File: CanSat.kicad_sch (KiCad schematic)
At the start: 46 parts, among them IC1 W25Q128JVPIQ, J1 USB_C_Receptacle, J10 Conn_01x04_Pin, J2 Conn_Coaxial, J3 Conn_01x06_Socket, J4 Conn_01x02_Pin, J5 Screw_Terminal_01x02, J6 Conn_01x06_Pin, J7 Conn_01x03_Pin, J8 Conn_01x02_Pin, J9 Conn_01x02_Pin, SW1 SW_Push, SW2 SW_Push, SW3 SW_Push, U1 MPU-6050, U3 Waveshare23721, U4 RFM98W-433S2, U8 BMP280, U9 APS6404L-3SQR-ZR

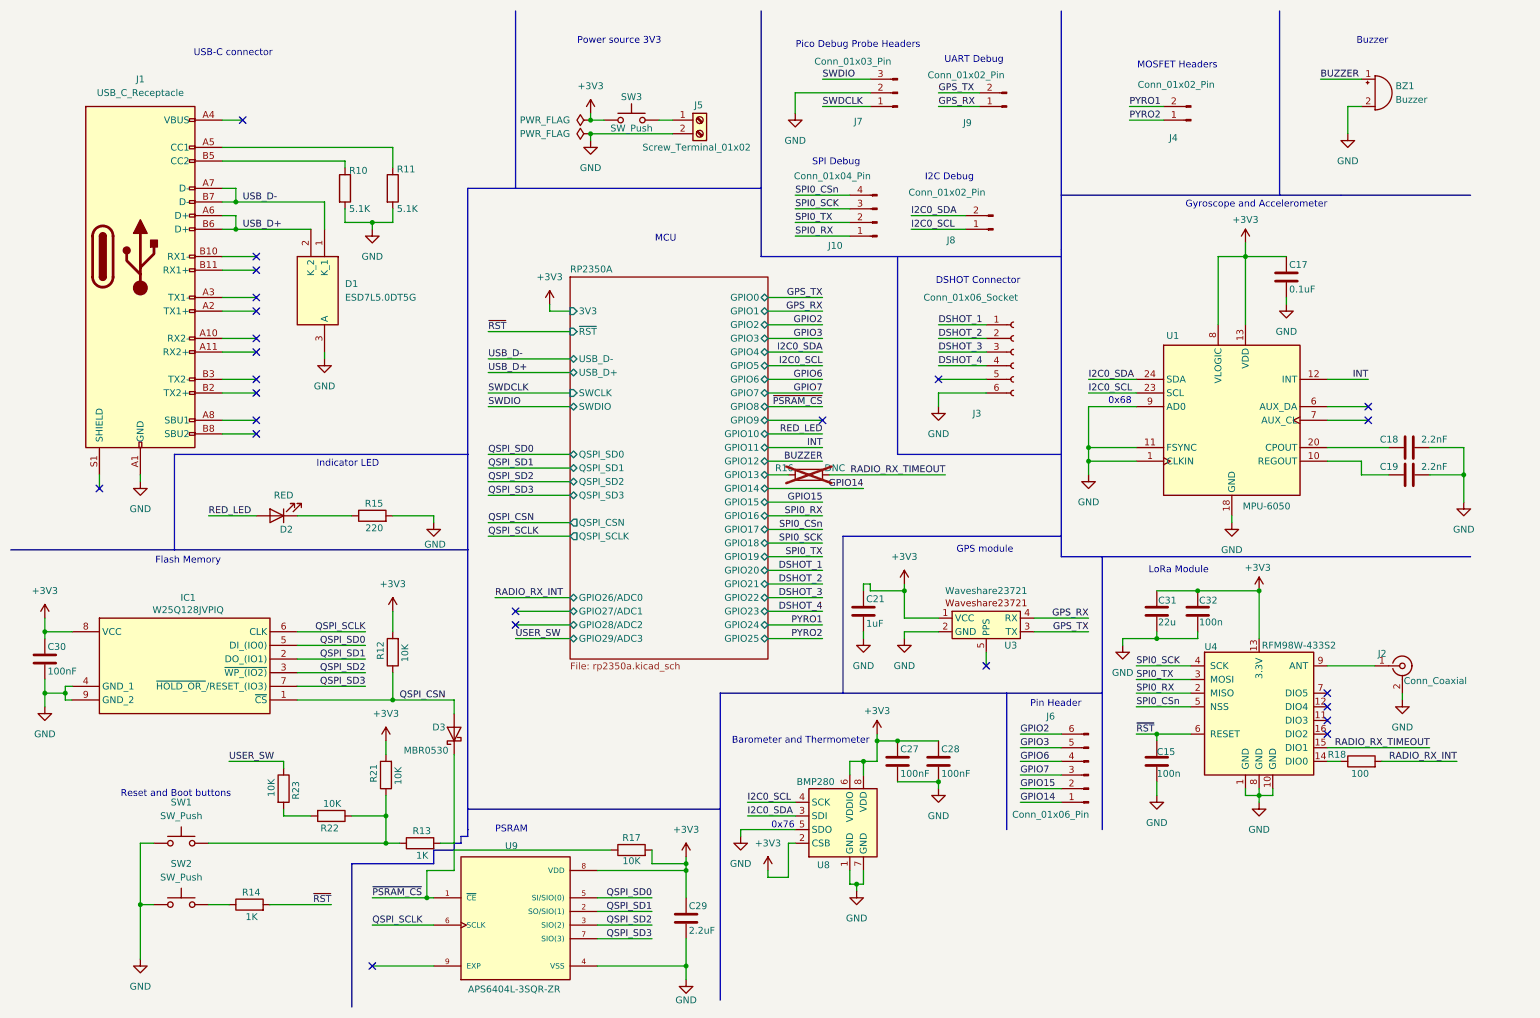
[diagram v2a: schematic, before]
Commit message: Changed connectors
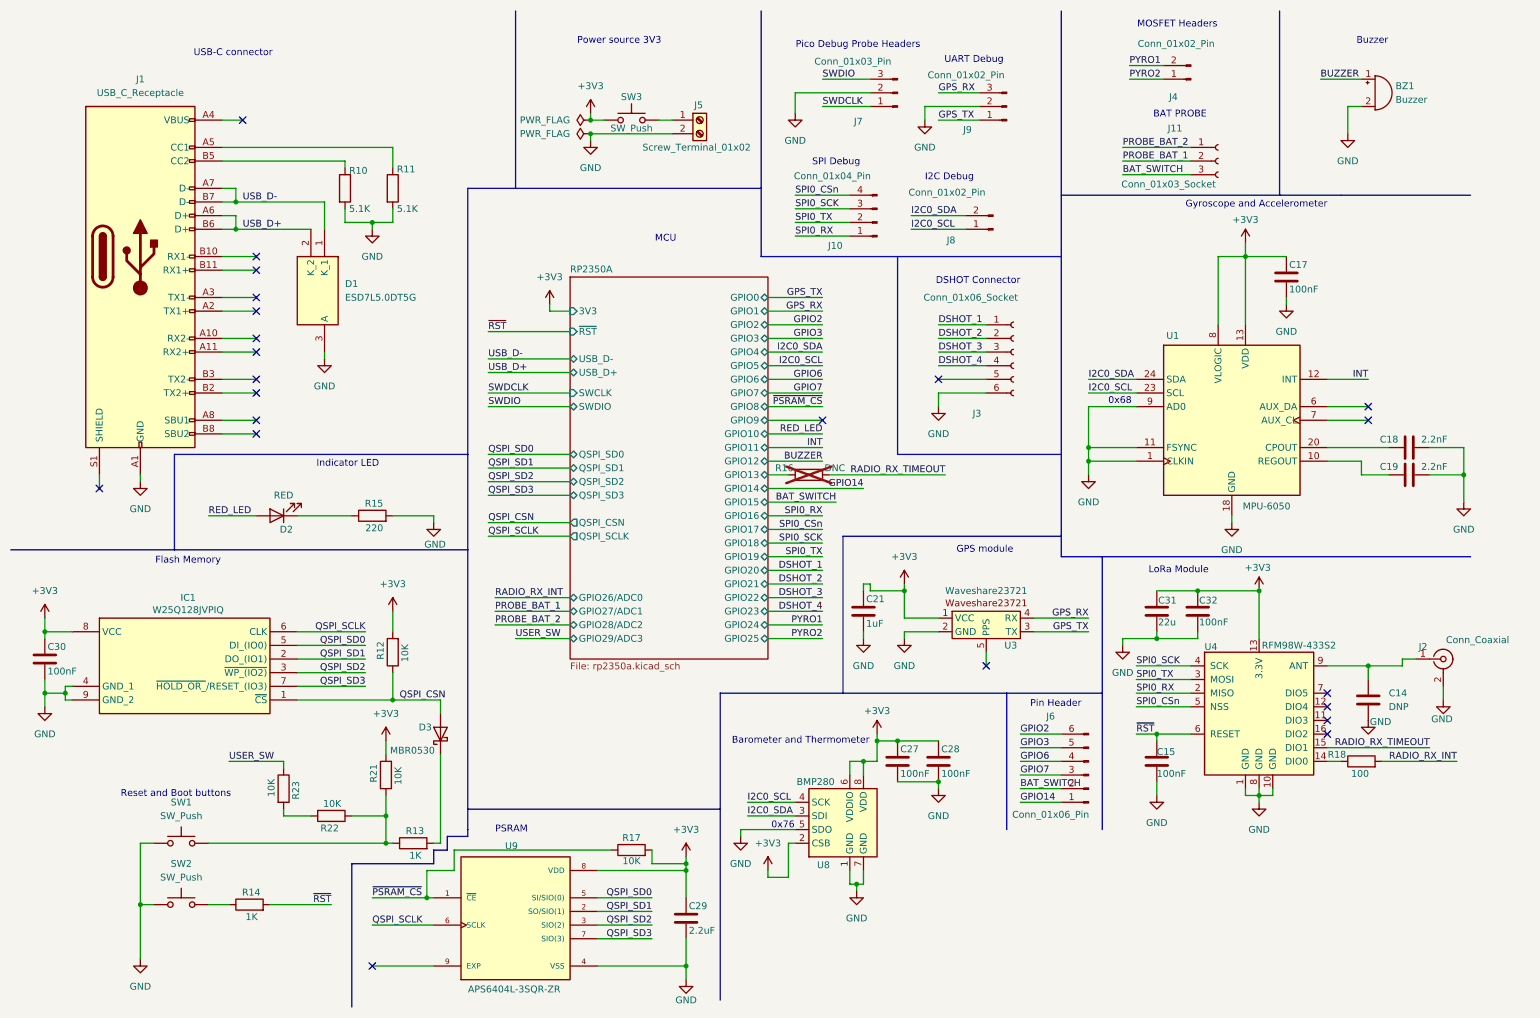
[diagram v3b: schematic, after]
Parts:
- added C14: DNP, Capacitor_SMD:C_0805_2012Metric, symbol Device:C
- added J11: Conn_01x03_Socket, Connector_JST:JST_PH_B3B-PH-K_1x03_P2.00mm_Vertical, symbol Connector:Conn_01x03_Socket
- C15, C32: value 100n -> 100nF
- C17: value 0.1uF -> 100nF
- J10: footprint Connector_PinHeader_1.00mm:PinHeader_1x04_P1.00mm_Vertical -> Connector_PinHeader_2.00mm:PinHeader_1x04_P2.00mm_Vertical
- J4: footprint Connector_PinHeader_1.00mm:PinHeader_1x02_P1.00mm_Vertical -> Connector_JST:JST_PH_B2B-PH-K_1x02_P2.00mm_Vertical
- J5: footprint TerminalBlock:TerminalBlock_bornier-2_P5.08mm -> Connector_JST:JST_PH_B2B-PH-K_1x02_P2.00mm_Vertical
- J7: footprint Connector_PinHeader_1.00mm:PinHeader_1x03_P1.00mm_Vertical -> Connector_JST:JST_SH_BM03B-SRSS-TB_1x03-1MP_P1.00mm_Vertical
- J8: footprint Connector_PinHeader_1.00mm:PinHeader_1x02_P1.00mm_Vertical -> Connector_PinHeader_2.00mm:PinHeader_1x02_P2.00mm_Vertical
- J9: footprint Connector_PinHeader_1.00mm:PinHeader_1x02_P1.00mm_Vertical -> Connector_JST:JST_SH_BM03B-SRSS-TB_1x03-1MP_P1.00mm_Vertical; symbol Connector:Conn_01x02_Pin -> Connector:Conn_01x03_Pin
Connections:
- net GND: now also J9.2 (Pin_2), C14.1
- net GPS_RX: now also J9.3 (Pin_3); no longer J9.1 (Pin_1)
- net GPS_TX: now also J9.1 (Pin_1); no longer J9.2 (Pin_2)
- net at J2.1 (In), U4.9 (ANT): now also C14.2
- net GPIO15 renamed BAT_SWITCH
- net BAT_SWITCH: now also J11.3 (Pin_3)
- new net PROBE_BAT_1: J11.2 (Pin_2)
- new net PROBE_BAT_2: J11.1 (Pin_1)
- no-connect marks 24 -> 22
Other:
- note added: "BAT PROBE"
- moved on the sheet: D3, J2, J4, R13

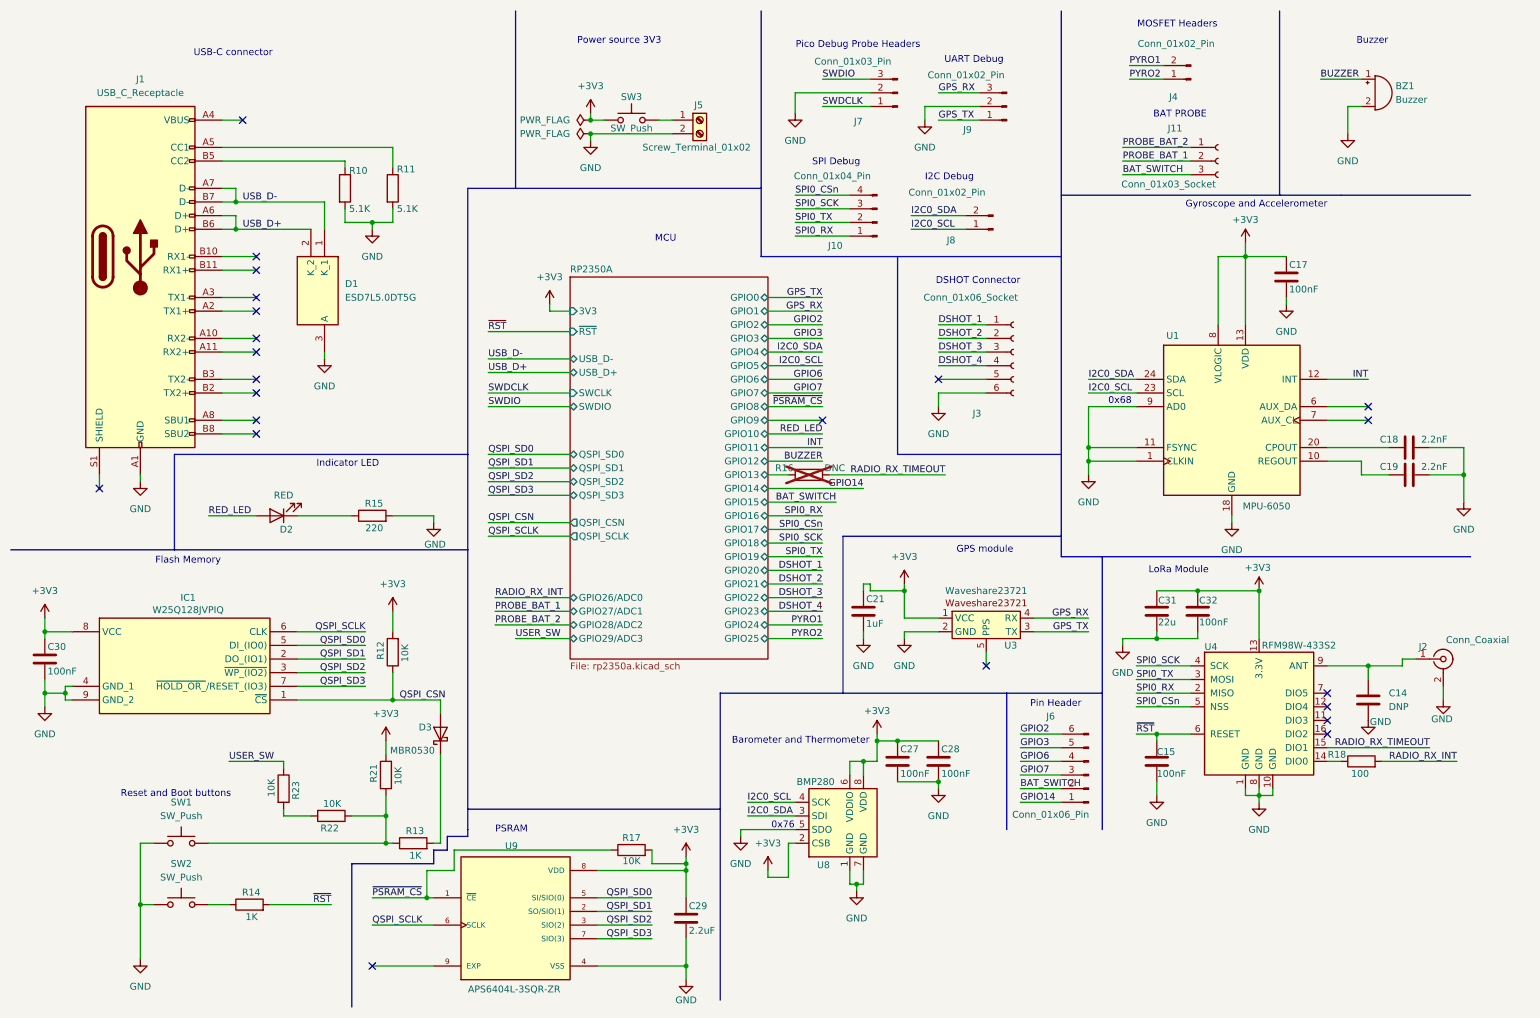
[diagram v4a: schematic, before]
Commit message: changed buzzer circuit and capacitor footprints
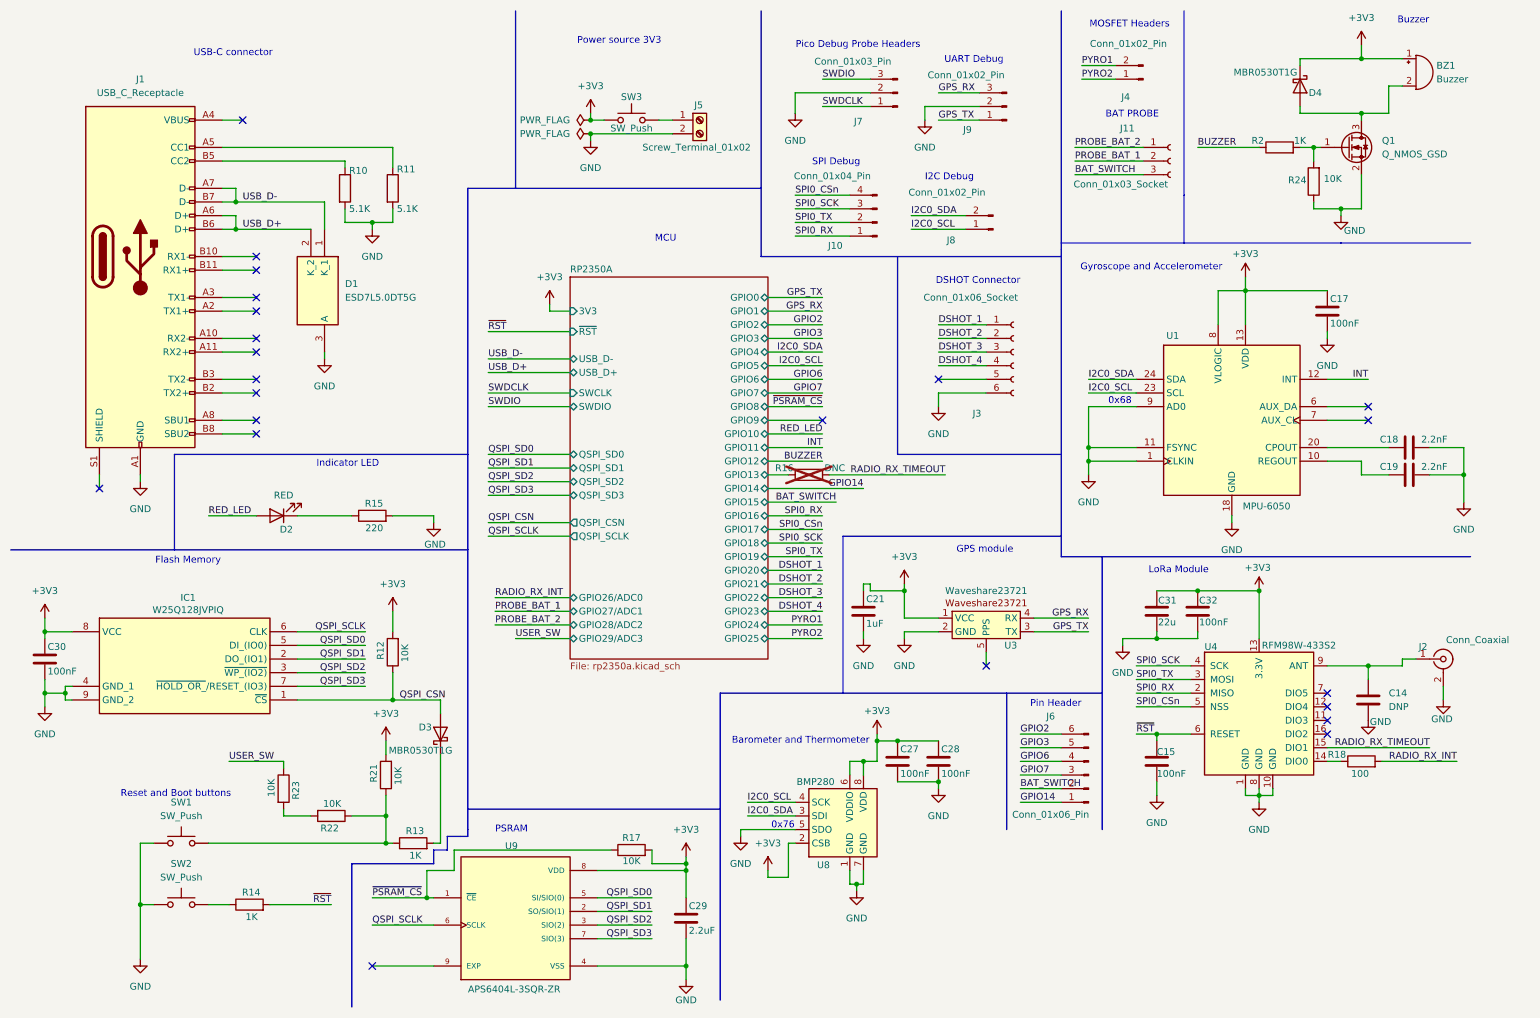
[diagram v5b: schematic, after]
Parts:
- added D4: MBR0530T1G, Diode_SMD:D_SOD-123, symbol Diode:MBR0530
- added Q1: Q_NMOS_GSD, Package_TO_SOT_SMD:SOT-23, symbol Transistor_FET:Q_NMOS_GSD
- added R2: 1K, Resistor_SMD:R_0805_2012Metric, symbol Device:R
- added R24: 10K, Resistor_SMD:R_0805_2012Metric, symbol Device:R
- C15, C17, C18, C19, C21, C27, C28, C29, C30, C31, C32: footprint Capacitor_Tantalum_SMD:CP_EIA-2012-15_AVX-P -> Capacitor_SMD:C_0805_2012Metric
- D3: value MBR0530 -> MBR0530T1G
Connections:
- net +3V3: now also BZ1.1 (+), D4.1 (K)
- net BUZZER: now also R2.1; no longer BZ1.1 (+)
- net GND: now also Q1.2 (S), R24.1; no longer BZ1.2 (-)
- new net: BZ1.2 (-), D4.2 (A), Q1.3 (D)
- new net: Q1.1 (G), R2.2, R24.2
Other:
- moved on the sheet: BZ1, C17, J11, J4

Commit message: added Q1 part number
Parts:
- Q1: value Q_NMOS_GSD -> BSS138
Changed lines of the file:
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@@
 			)
 		)
-		(property "Value" "Q_NMOS_GSD"
+		(property "Value" "BSS138"
 			(at 267.97 39.3699 0)
 			(effects

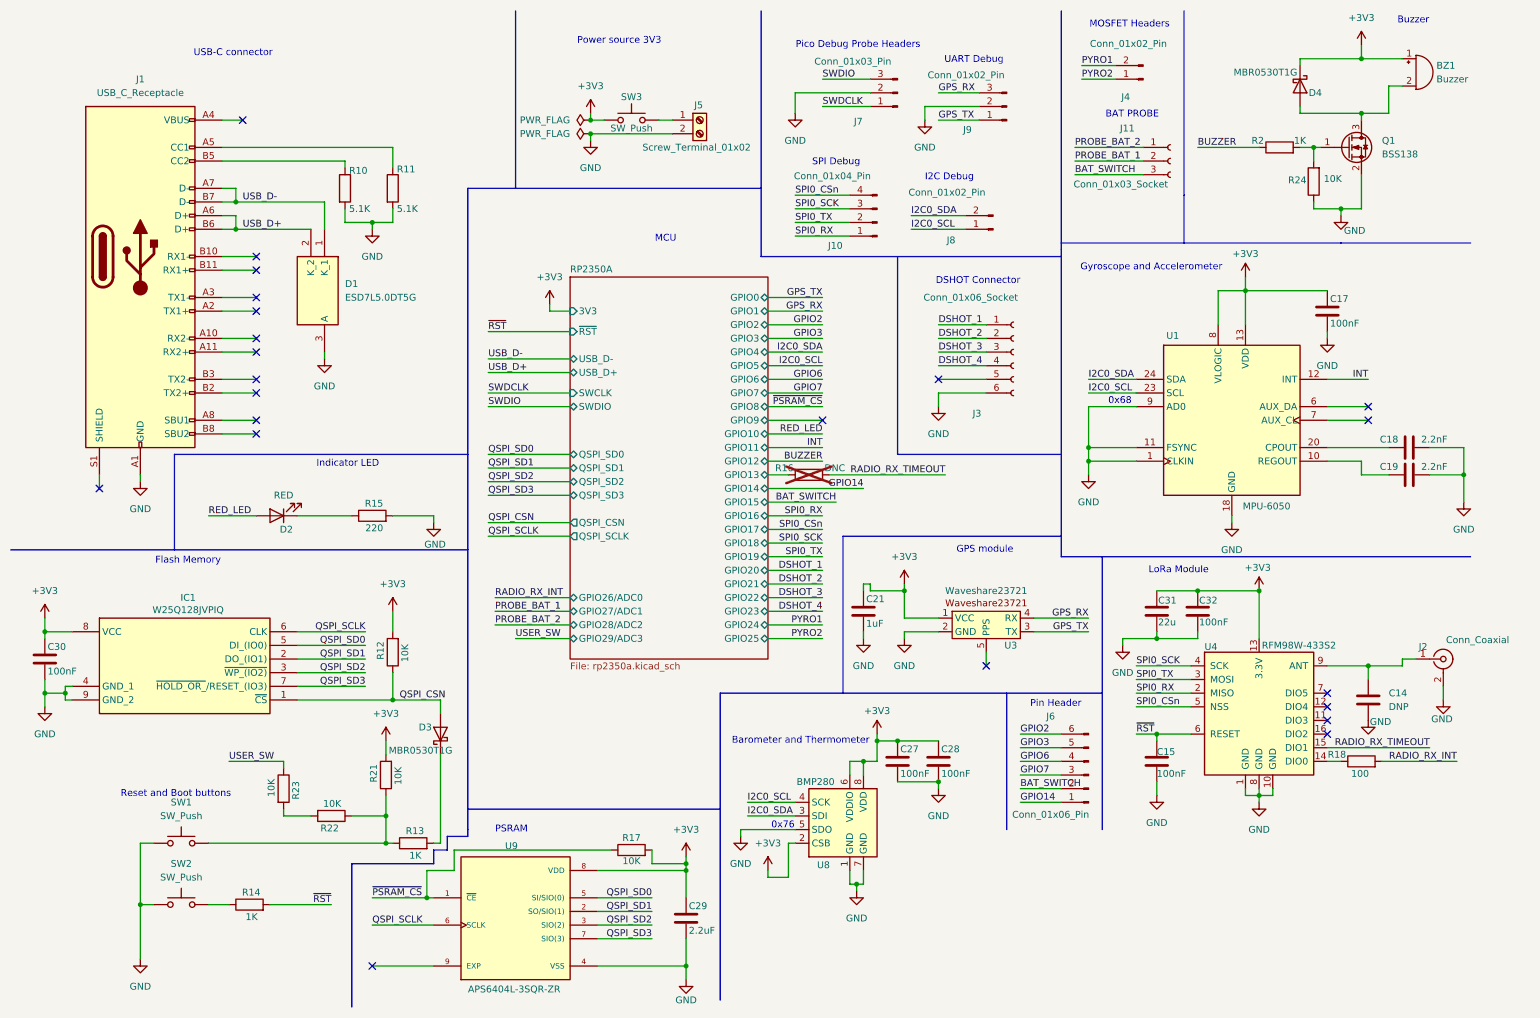
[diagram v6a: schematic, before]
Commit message: Changed QSPI and added pull-ups on i2c
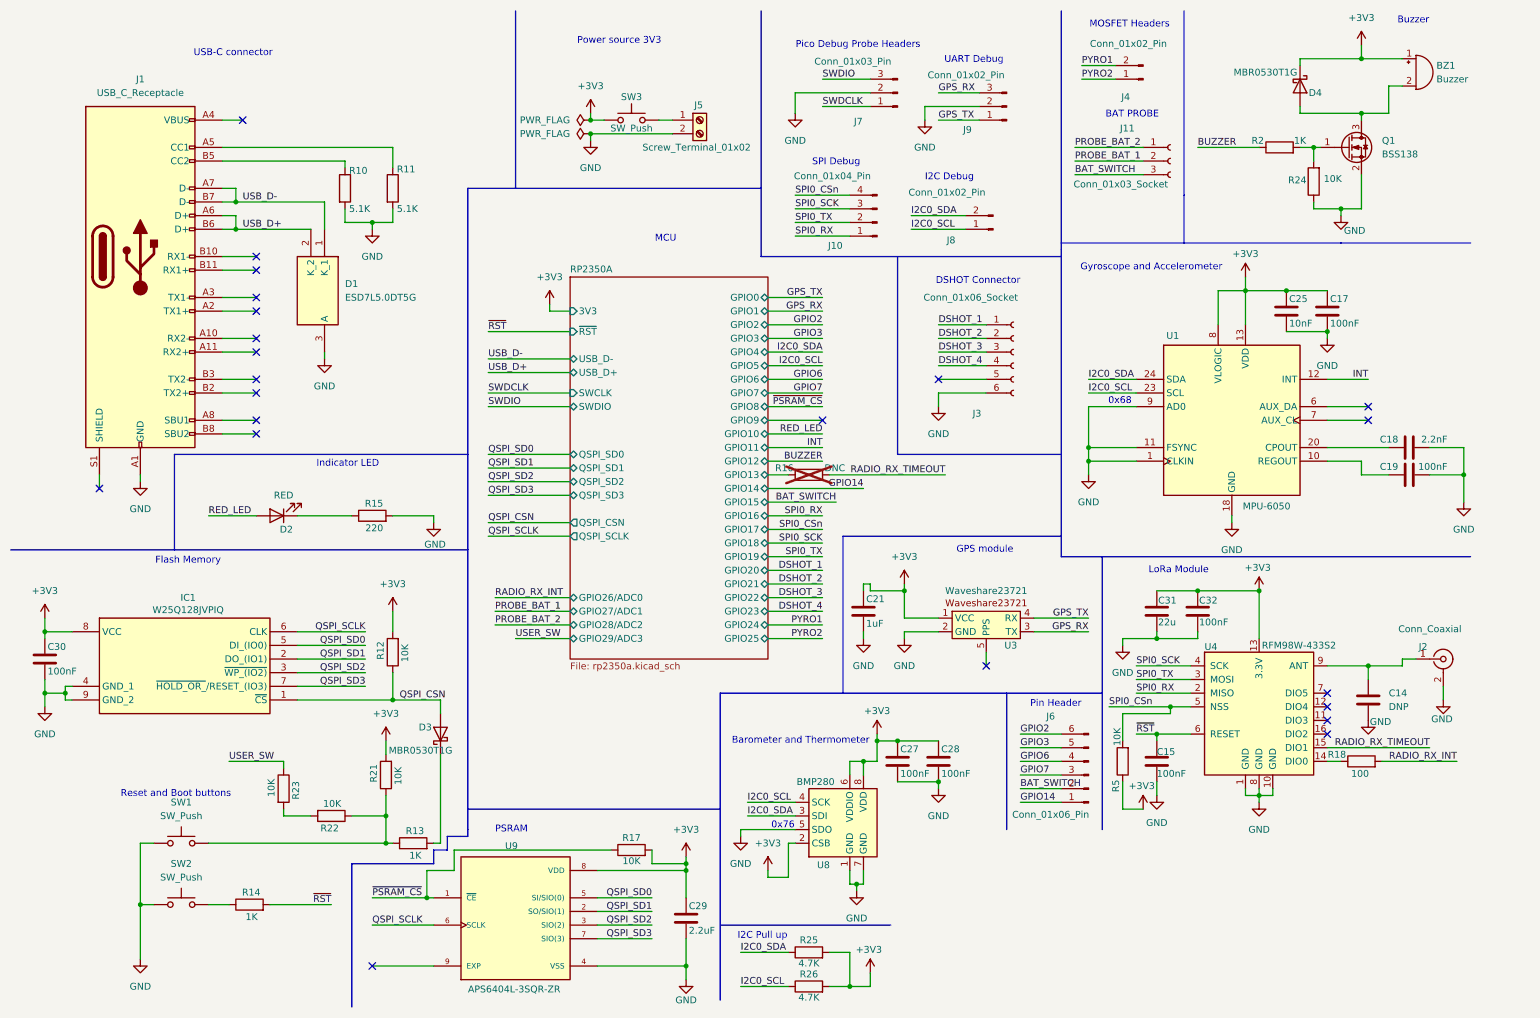
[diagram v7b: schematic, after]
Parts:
- added C25: 10nF, Capacitor_SMD:C_0805_2012Metric, symbol Device:C
- added R25, R26: 4.7K, Resistor_SMD:R_0402_1005Metric, symbol Device:R
- added R5: 10K, Resistor_SMD:R_0805_2012Metric, symbol Device:R
- C19: value 2.2nF -> 100nF
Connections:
- net +3V3: now also C25.1, R25.2, R26.2, R5.1
- net GND: now also C25.2
- net GPS_RX: now also U3.3 (TX); no longer U3.4 (RX)
- net GPS_TX: now also U3.4 (RX); no longer U3.3 (TX)
- net I2C0_SCL: now also R26.1
- net I2C0_SDA: now also R25.1
- net SPI0_CSn: now also R5.2
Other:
- note added: "I2C Pull up"
